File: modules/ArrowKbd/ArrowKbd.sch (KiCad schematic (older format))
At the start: 42 parts, among them J1 2, J10 11, J11 12, J12 13, J13 A0, J14 A1, J15 A2, J16 A3, J17 A4, J18 A5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

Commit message: Arrow Kbd ready
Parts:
- R1, R2, R3: value R -> 10k
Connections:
- wire segments 36 -> 52
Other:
- moved on the sheet: JP1, R3, U1A, U1B
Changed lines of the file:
@@
 L 74xx_IEEE:74LS139 U1
 U 1 1 5E5D5B2D
+P 2225 5375
+F 0 "U1" H 2050 5825 50  0000 C CNN
+F 1 "74LS139" H 2425 5825 50  0000 C CNN
+F 2 "Package_SO:SOIC-16_3.9x9.9mm_P1.27mm" H 2225 5375 50  0001 C CNN
+F 3 "" H 2225 5375 50  0001 C CNN
+	1    2225 5375
+	1    0    0    -1
+$EndComp
+$Comp
+L 74xx_IEEE:74LS139 U1
+U 2 1 5E5D6291
 P 2225 4250
-F 0 "U1" H 2050 4700 50  0000 C CNN
-F 1 "74LS139" H 2425 4700 50  0000 C CNN
+F 0 "U1" H 2225 4866 50  0000 C CNN
+F 1 "74LS139" H 2225 4775 50  0000 C CNN
 F 2 "Package_SO:SOIC-16_3.9x9.9mm_P1.27mm" H 2225 4250 50  0001 C CNN
 F 3 "" H 2225 4250 50  0001 C CNN
-	1    2225 4250
-	1    0    0    -1
-$EndComp
-$Comp
-L 74xx_IEEE:74LS139 U1
-U 2 1 5E5D6291
-P 6525 5525
-F 0 "U1" H 6525 6141 50  0000 C CNN
-F 1 "74LS139" H 6525 6050 50  0000 C CNN
-F 2 "Package_SO:SOIC-16_3.9x9.9mm_P1.27mm" H 6525 5525 50  0001 C CNN
-F 3 "" H 6525 5525 50  0001 C CNN
-	2    6525 5525
+	2    2225 4250
 	1    0    0    -1
 $EndComp
@@
 	3200 4500 3400 4500
 Wire Wire Line
-	1225 4000 1675 4000
-Wire Wire Line
-	1225 4150 1675 4150
+	1225 4000 1550 4000
+Wire Wire Line
+	1225 4150 1450 4150
 $Comp
 L power:GND #PWR01001
@@
 Wire Wire Line
 	1675 4500 1675 4575
-Wire Wire Line
-	5975 5275 5975 5425
-Wire Wire Line
-	5975 5425 5975 5775
-Connection ~ 5975 5425
 $Comp
 L Device:R R3
 U 1 1 5E5ED801
-P 5975 5125
-F 0 "R3" H 6045 5171 50  0000 L CNN
-F 1 "R" H 6045 5080 50  0000 L CNN
-F 2 "Resistor_SMD:R_0805_2012Metric_Pad1.15x1.40mm_HandSolder" V 5905 5125 50  0001 C CNN
-F 3 "~" H 5975 5125 50  0001 C CNN
-	1    5975 5125
-	1    0    0    -1
-$EndComp
-Connection ~ 5975 5275
+P 1675 5775
+F 0 "R3" H 1745 5821 50  0000 L CNN
+F 1 "10k" H 1745 5730 50  0000 L CNN
+F 2 "Resistor_SMD:R_0805_2012Metric_Pad1.15x1.40mm_HandSolder" V 1605 5775 50  0001 C CNN
+F 3 "~" H 1675 5775 50  0001 C CNN
+	1    1675 5775
+	1    0    0    -1
+$EndComp
 $Comp
 L power:VCC #PWR01004
 U 1 1 5E5EE355
-P 5975 4900
-F 0 "#PWR01004" H 5975 4750 50  0001 C CNN
-F 1 "VCC" H 5992 5073 50  0000 C CNN
-F 2 "" H 5975 4900 50  0001 C CNN
-F 3 "" H 5975 4900 50  0001 C CNN
-	1    5975 4900
-	1    0    0    -1
+P 1675 5925
+F 0 "#PWR01004" H 1675 5775 50  0001 C CNN
+F 1 "VCC" H 1692 6098 50  0000 C CNN
+F 2 "" H 1675 5925 50  0001 C CNN
+F 3 "" H 1675 5925 50  0001 C CNN
+	1    1675 5925
+	-1   0    0    1
 $EndComp
 Wire Wire Line
@@
 P 3800 3700
 F 0 "R1" H 3870 3746 50  0000 L CNN
-F 1 "R" H 3870 3655 50  0000 L CNN
+F 1 "10k" H 3870 3655 50  0000 L CNN
 F 2 "Resistor_SMD:R_0805_2012Metric_Pad1.15x1.40mm_HandSolder" V 3730 3700 50  0001 C CNN
 F 3 "~" H 3800 3700 50  0001 C CNN
@@
 P 3800 5650
 F 0 "R2" H 3870 5696 50  0000 L CNN
-F 1 "R" H 3870 5605 50  0000 L CNN
+F 1 "10k" H 3870 5605 50  0000 L CNN
 F 2 "Resistor_SMD:R_0805_2012Metric_Pad1.15x1.40mm_HandSolder" V 3730 5650 50  0001 C CNN
 F 3 "~" H 3800 5650 50  0001 C CNN
@@
 L Jumper:Jumper_3_Bridged12 JP1
 U 1 1 5E5F8826
-P 5225 2775
-F 0 "JP1" H 5225 2979 50  0000 C CNN
-F 1 "Jumper_3_Bridged12" H 5225 2888 50  0000 C CNN
-F 2 "Connector_PinHeader_2.54mm:PinHeader_1x03_P2.54mm_Vertical" H 5225 2775 50  0001 C CNN
-F 3 "~" H 5225 2775 50  0001 C CNN
-	1    5225 2775
-	1    0    0    -1
+P 2725 2925
+F 0 "JP1" H 2725 3129 50  0000 C CNN
+F 1 "Jumper_3_Bridged12" H 2725 3038 50  0000 C CNN
+F 2 "Connector_PinHeader_2.54mm:PinHeader_1x03_P2.54mm_Vertical" H 2725 2925 50  0001 C CNN
+F 3 "~" H 2725 2925 50  0001 C CNN
+	1    2725 2925
+	0    -1   -1   0
 $EndComp
 $Comp
@@
 	1    0    0    -1
 $EndComp
+Wire Wire Line
+	1225 3550 2725 3550
+Wire Wire Line
+	2725 3550 2725 3175
+Wire Wire Line
+	2725 2675 2725 2450
+Wire Wire Line
+	2725 2450 2425 2450
+Wire Wire Line
+	2425 2450 2425 3400
+Wire Wire Line
+	2425 3400 1225 3400
+Wire Wire Line
+	2875 2925 4500 2925
+Wire Wire Line
+	4500 2925 4500 4500
+Wire Wire Line
+	4500 4500 3800 4500
+Connection ~ 3800 4500
+Wire Wire Line
+	6750 2950 4750 2950
+Wire Wire Line
+	4750 2950 4750 4850
+Wire Wire Line
+	4750 4850 3800 4850
+Connection ~ 3800 4850
+Wire Wire Line
+	1675 5125 1550 5125
+Wire Wire Line
+	1550 5125 1550 4000
+Connection ~ 1550 4000
+Wire Wire Line
+	1550 4000 1675 4000
+Wire Wire Line
+	1675 5275 1450 5275
+Wire Wire Line
+	1450 5275 1450 4150
+Connection ~ 1450 4150
+Wire Wire Line
+	1450 4150 1675 4150
 $EndSCHEMATC

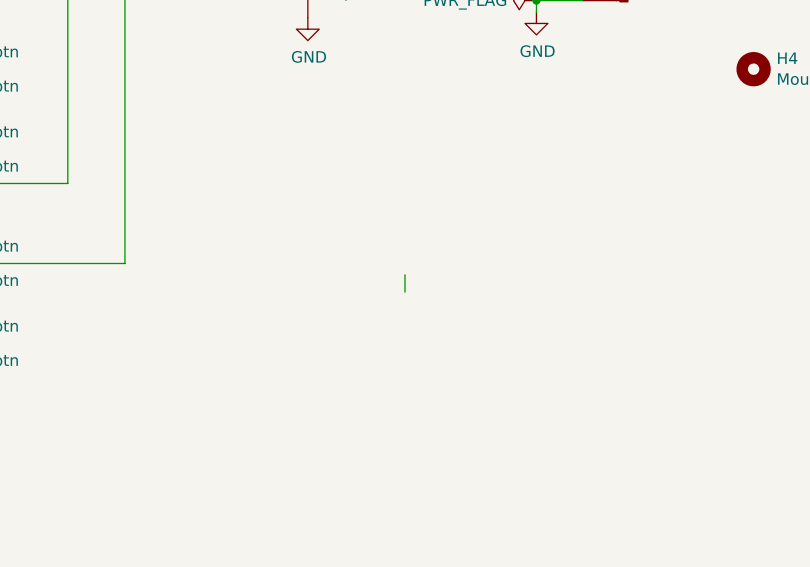
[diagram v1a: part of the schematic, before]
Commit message: Add date. Add polygon.
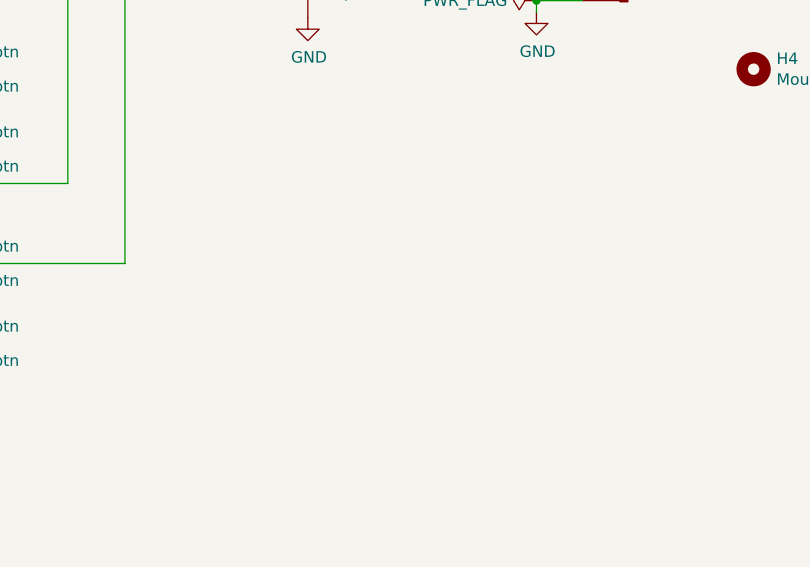
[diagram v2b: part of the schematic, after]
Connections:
- wire segments 52 -> 51
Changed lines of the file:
@@
 	-1   0    0    1
 $EndComp
-Wire Wire Line
-	5975 4900 5975 4975
 $Comp
 L Device:R R1

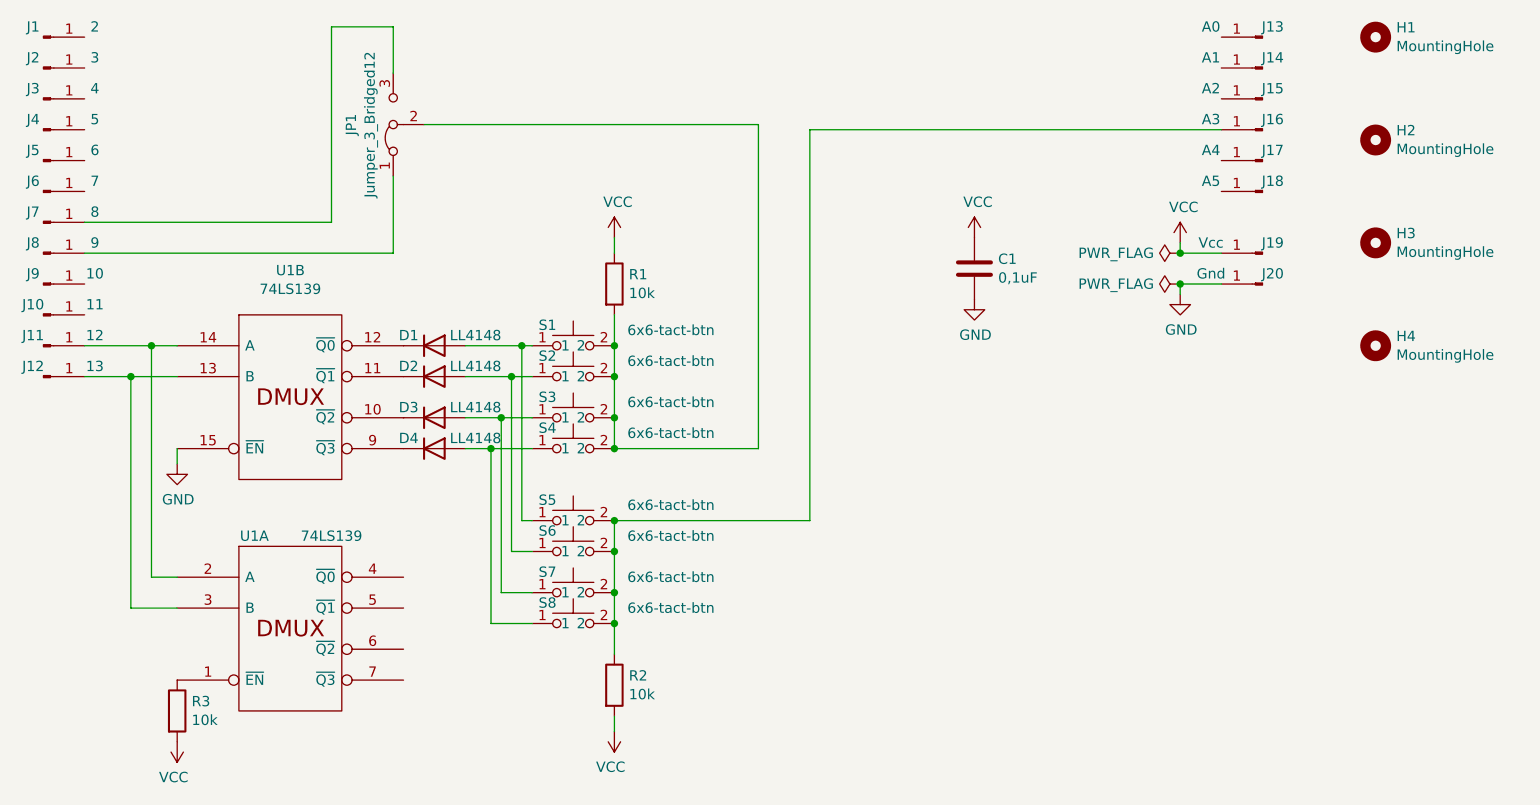
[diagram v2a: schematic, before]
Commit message: ArrowKbd v2. Change pin assigning
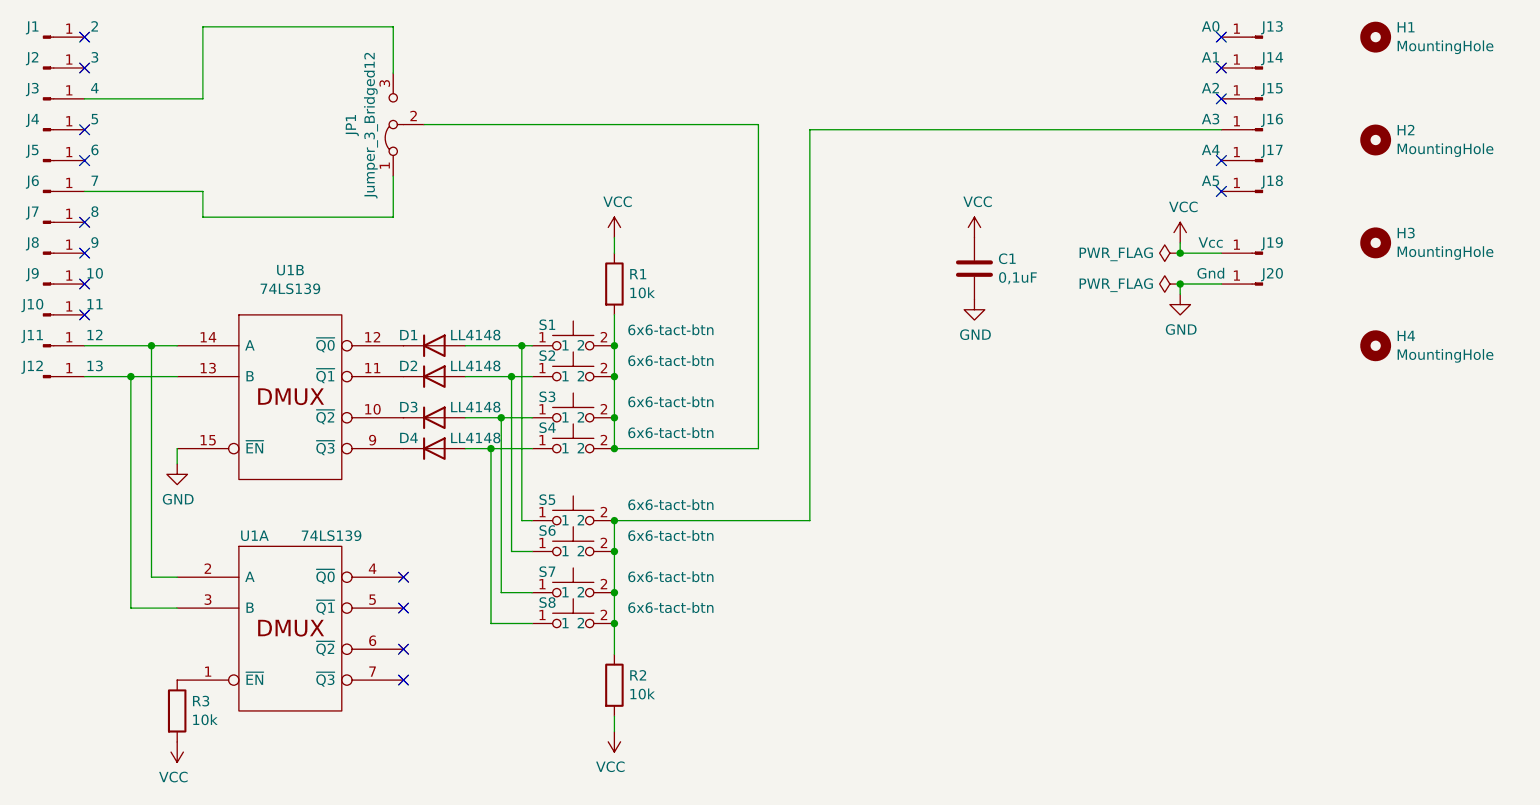
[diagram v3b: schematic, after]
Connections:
- net at J3.1 (Pin_1): now also JP1.3 (B)
- net at J6.1 (Pin_1): now also JP1.1 (A)
- net at J7.1 (Pin_1): no longer JP1.3 (B)
- net at J8.1 (Pin_1): no longer JP1.1 (A)
- no-connect marks 0 -> 17
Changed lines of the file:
@@
 EESchema Schematic File Version 4
-LIBS:ArrowKbd-cache
 EELAYER 30 0
 EELAYER END
@@
 $EndComp
 Wire Wire Line
-	1225 3550 2725 3550
-Wire Wire Line
-	2725 3550 2725 3175
-Wire Wire Line
 	2725 2675 2725 2450
-Wire Wire Line
-	2725 2450 2425 2450
-Wire Wire Line
-	2425 2450 2425 3400
-Wire Wire Line
-	2425 3400 1225 3400
 Wire Wire Line
 	2875 2925 4500 2925
@@
 Wire Wire Line
 	1450 4150 1675 4150
+Wire Wire Line
+	1225 2800 1800 2800
+Wire Wire Line
+	1800 2800 1800 2450
+Wire Wire Line
+	1800 2450 2725 2450
+Wire Wire Line
+	1225 3250 1800 3250
+Wire Wire Line
+	1800 3250 1800 3375
+Wire Wire Line
+	1800 3375 2725 3375
+Wire Wire Line
+	2725 3375 2725 3175
+NoConn ~ 1225 2500
+NoConn ~ 1225 2650
+NoConn ~ 1225 2950
+NoConn ~ 1225 3100
+NoConn ~ 1225 3400
+NoConn ~ 1225 3550
+NoConn ~ 1225 3700
+NoConn ~ 1225 3850
+NoConn ~ 2775 5125
+NoConn ~ 2775 5275
+NoConn ~ 2775 5475
+NoConn ~ 2775 5625
+NoConn ~ 6750 2500
+NoConn ~ 6750 2650
+NoConn ~ 6750 2800
+NoConn ~ 6750 3100
+NoConn ~ 6750 3250
 $EndSCHEMATC

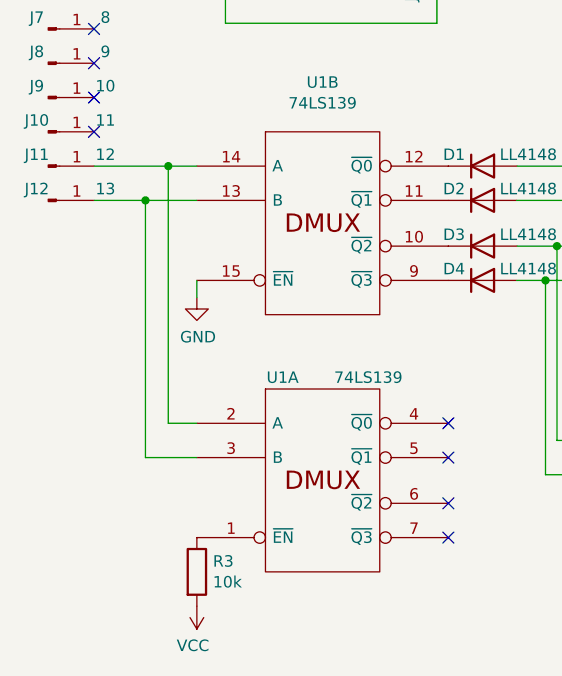
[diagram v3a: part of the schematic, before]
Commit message: Fix 74LS139 pins
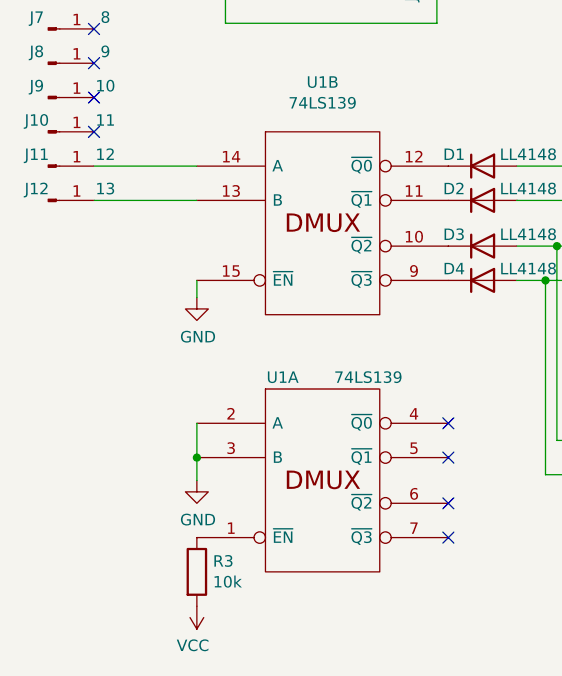
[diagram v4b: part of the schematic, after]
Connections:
- net GND: now also U1.2 (A), U1.3 (B)
- net at J11.1 (Pin_1), U1.14 (A): no longer U1.2 (A)
- net at J12.1 (Pin_1), U1.13 (B): no longer U1.3 (B)
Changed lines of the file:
@@
 Wire Wire Line
 	3200 4500 3400 4500
-Wire Wire Line
-	1225 4000 1550 4000
-Wire Wire Line
-	1225 4150 1450 4150
 $Comp
 L power:GND #PWR01001
@@
 	4750 4850 3800 4850
 Connection ~ 3800 4850
-Wire Wire Line
-	1675 5125 1550 5125
-Wire Wire Line
-	1550 5125 1550 4000
-Connection ~ 1550 4000
-Wire Wire Line
-	1550 4000 1675 4000
-Wire Wire Line
-	1675 5275 1450 5275
-Wire Wire Line
-	1450 5275 1450 4150
-Connection ~ 1450 4150
-Wire Wire Line
-	1450 4150 1675 4150
 Wire Wire Line
 	1225 2800 1800 2800
@@
 NoConn ~ 6750 3100
 NoConn ~ 6750 3250
+Wire Wire Line
+	1225 4000 1675 4000
+Wire Wire Line
+	1225 4150 1675 4150
+$Comp
+L power:GND #PWR?
+U 1 1 5FA6E132
+P 1675 5375
+F 0 "#PWR?" H 1675 5125 50  0001 C CNN
+F 1 "GND" H 1680 5202 50  0000 C CNN
+F 2 "" H 1675 5375 50  0001 C CNN
+F 3 "" H 1675 5375 50  0001 C CNN
+	1    1675 5375
+	1    0    0    -1
+$EndComp
+Wire Wire Line
+	1675 5125 1675 5275
+Wire Wire Line
+	1675 5375 1675 5275
+Connection ~ 1675 5275
 $EndSCHEMATC
